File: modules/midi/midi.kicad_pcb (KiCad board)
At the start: 2 copper layers, 30.5 x 68.6 mm, 57 parts, among them J1 MIDI_IN, U1 ATtiny1616-M

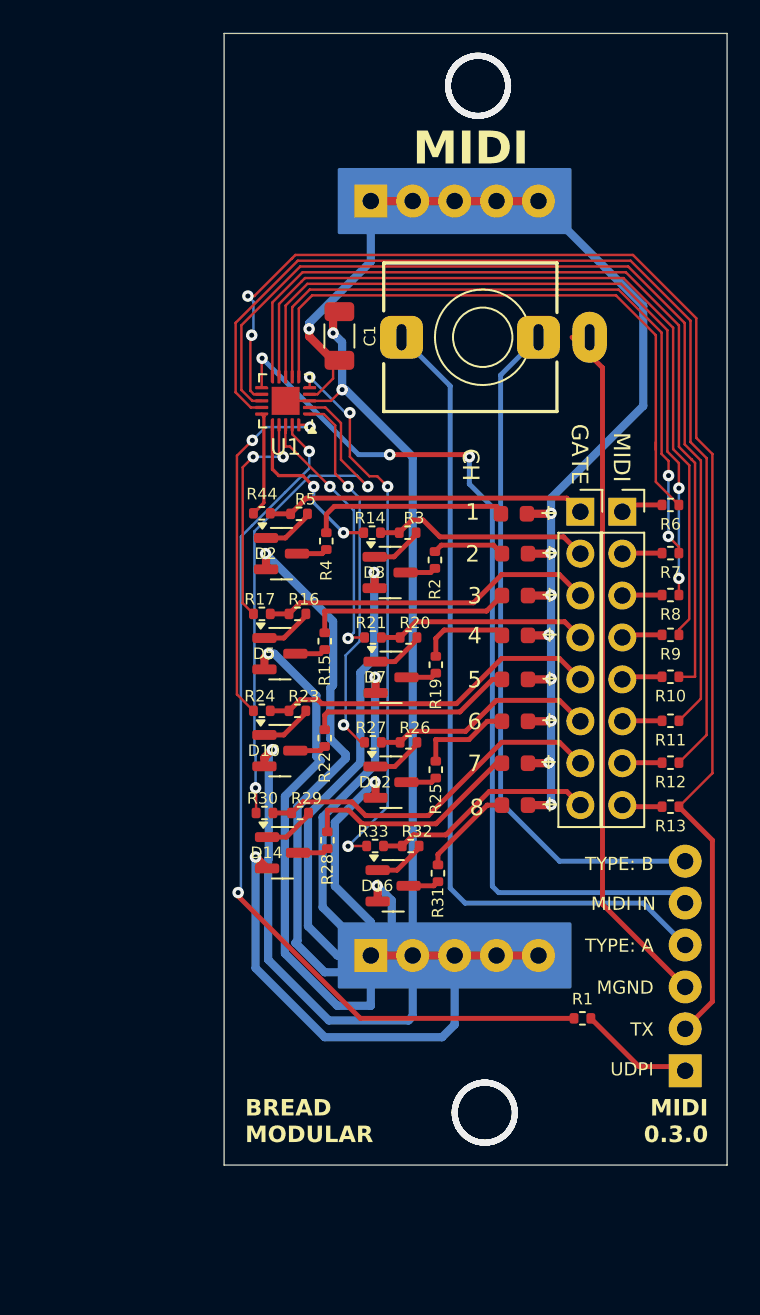
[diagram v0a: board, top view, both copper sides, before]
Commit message: midi: Connect MIDI ground to common GND
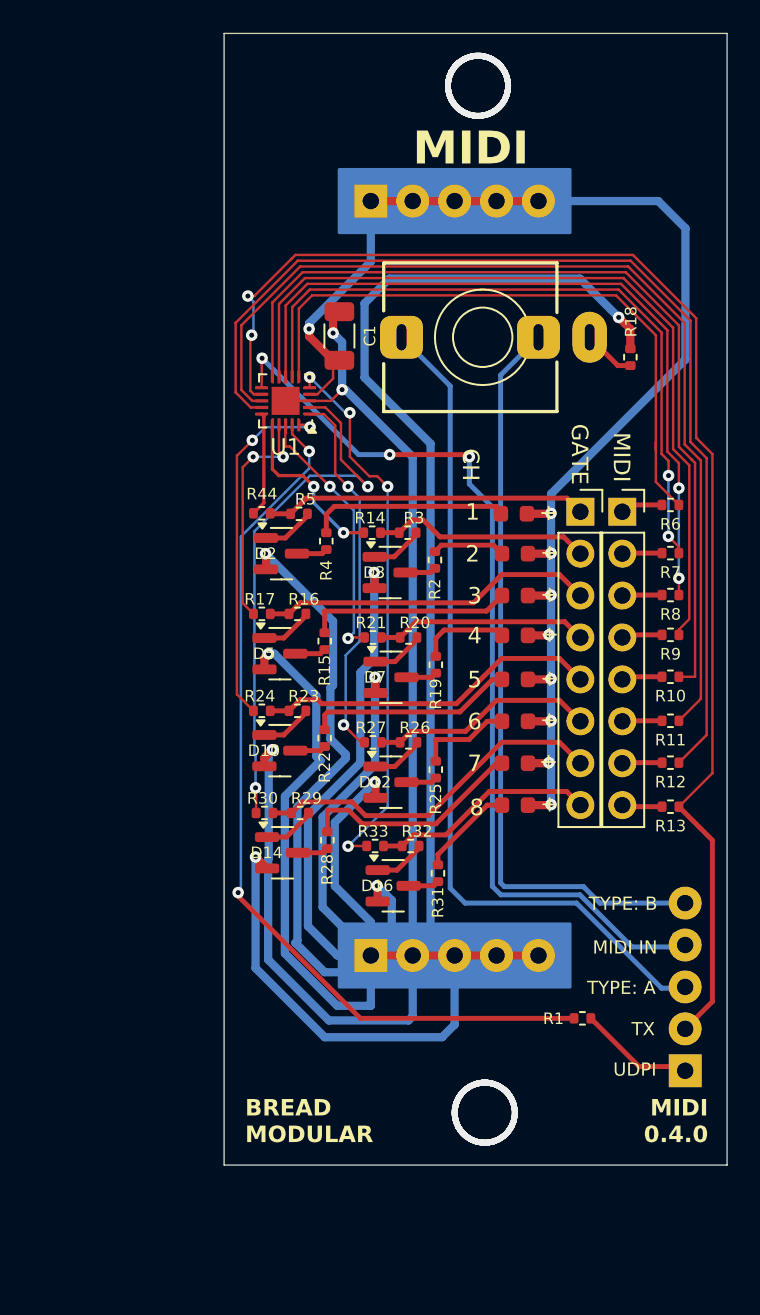
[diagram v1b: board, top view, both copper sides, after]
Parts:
- added R18: 10k, Resistor_SMD:R_0402_1005Metric, F.Cu at (71.6, 60.3)
- CONFIG1: footprint BreadModular_MISC:Conn_Holes_6 -> BreadModular_MISC:Power_Connector
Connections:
- CONFIG1 pad 3: MIDI_GROUND -> MIDI_DATA_TYPE_A
- CONFIG1 pad 4: MIDI_DATA_TYPE_A -> MIDI_IN
- CONFIG1 pad 5: MIDI_IN -> MIDI_DATA_TYPE_B
- J1 pad S: MIDI_GROUND -> Net-(J1-PadS)
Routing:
- net GND: track 242.4 -> 303.1 mm, vias 10 -> 11
- net MIDI_GROUND: track 42.3 -> 0.00 mm
- net V_SUPPLY: track 77.5 -> 83.9 mm
- net MIDI_DATA_TYPE_B: track 41.8 -> 45.7 mm
- net Net-(J1-PadS): track 0.00 -> 3.18 mm
- net MIDI_IN: track 55.3 -> 57.3 mm
- net MIDI_DATA_TYPE_A: track 50.0 -> 51.4 mm
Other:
- board text added: "MIDI 0.4.0"
- board text removed: "MGND"
- board text removed: "MIDI 0.3.0"

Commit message: midi: fix instability in MIDI recieving
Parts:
- removed R18: 10k, Resistor_SMD:R_0402_1005Metric
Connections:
- J1 pad S: Net-(J1-PadS) -> GND
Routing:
- net Net-(J1-PadS): track 3.18 -> 0.00 mm
- net GND: track 303.1 -> 301.7 mm, vias 11 -> 10
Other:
- board text added: "MIDI 0.5.0"
- board text removed: "MIDI 0.4.0"
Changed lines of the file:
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@@
 	(net 62 "Net-(D100-K)")
 	(net 63 "MIDI_DATA_TYPE_A")
-	(net 64 "Net-(J1-PadS)")
 	(footprint "LED_SMD:LED_0603_1608Metric"
 		(layer "F.Cu")
@@
 			(layers "*.Cu" "*.Mask")
 			(remove_unused_layers no)
-			(net 64 "Net-(J1-PadS)")
+			(net 1 "GND")
 			(pintype "passive")
 		)
@@
 		)
 	)
-	(footprint "Resistor_SMD:R_0402_1005Metric"
-		(layer "F.Cu")
-		(at 71.61 60.26 90)
-		(descr "Resistor SMD 0402 (1005 Metric), square (rectangular) end terminal, IPC_7351 nominal, (Body size source: IPC-SM-782 page 72, https://www.pcb-3d.com/wordpress/wp-content/uploads/ipc-sm-782a_amendment_1_and_2.pdf), generated with kicad-footprint-generator")
-		(tags "resistor")
-		(property "Reference" "R18"
-			(at 2.15 0.04 90)
-			(layer "F.SilkS")
-			(effects
-				(font
-					(size 0.7 0.7)
-					(thickness 0.1)
-				)
-			)
-		)
-		(property "Value" "10k"
-			(at 0 1.17 90)
-			(layer "F.Fab")
-			(effects
-				(font
-					(size 1 1)
-					(thickness 0.15)
-				)
-			)
-		)
-		(property "Footprint" "Resistor_SMD:R_0402_1005Metric"
-			(at 0 0 90)
-			(unlocked yes)
-			(layer "F.Fab")
-			(hide yes)
-			(effects
-				(font
-					(size 1.27 1.27)
-					(thickness 0.15)
-				)
-			)
-		)
-		(property "Datasheet" ""
-			(at 0 0 90)
-			(unlocked yes)
-			(layer "F.Fab")
-			(hide yes)
-			(effects
-				(font
-					(size 1.27 1.27)
-					(thickness 0.15)
-				)
-			)
-		)
-		(property "Description" "Resistor"
-			(at 0 0 90)
-			(unlocked yes)
-			(layer "F.Fab")
-			(hide yes)
-			(effects
-				(font
-					(size 1.27 1.27)
-					(thickness 0.15)
-				)
-			)
-		)
-		(property ki_fp_filters "R_*")
-		(sheetname "Root")
-		(sheetfile "midi.kicad_sch")
-		(attr smd)
-		(fp_line
-			(start -0.153641 -0.38)
-			(end 0.153641 -0.38)
-			(stroke
-				(width 0.12)
-				(type solid)
-			)
-			(layer "F.SilkS")
-		)
-		(fp_line
-			(start -0.153641 0.38)
-			(end 0.153641 0.38)
-			(stroke
-				(width 0.12)
-				(type solid)
-			)
-			(layer "F.SilkS")
-		)
-		(fp_line
-			(start 0.93 -0.47)
-			(end 0.93 0.47)
-			(stroke
-				(width 0.05)
-				(type solid)
-			)
-			(layer "F.CrtYd")
-		)
-		(fp_line
-			(start -0.93 -0.47)
-			(end 0.93 -0.47)
-			(stroke
-				(width 0.05)
-				(type solid)
-			)
-			(layer "F.CrtYd")
-		)
-		(fp_line
-			(start 0.93 0.47)
-			(end -0.93 0.47)
-			(stroke
-				(width 0.05)
-				(type solid)
-			)
-			(layer "F.CrtYd")
-		)
-		(fp_line
-			(start -0.93 0.47)
-			(end -0.93 -0.47)
-			(stroke
-				(width 0.05)
-				(type solid)
-			)
-			(layer "F.CrtYd")
-		)
-		(fp_line
-			(start 0.525 -0.27)
-			(end 0.525 0.27)
-			(stroke
-				(width 0.1)
-				(type solid)
-			)
-			(layer "F.Fab")
-		)
-		(fp_line
-			(start -0.525 -0.27)
-			(end 0.525 -0.27)
-			(stroke
-				(width 0.1)
-				(type solid)
-			)
-			(layer "F.Fab")
-		)
-		(fp_line
-			(start 0.525 0.27)
-			(end -0.525 0.27)
-			(stroke
-				(width 0.1)
-				(type solid)
-			)
-			(layer "F.Fab")
-		)
-		(fp_line
-			(start -0.525 0.27)
-			(end -0.525 -0.27)
-			(stroke
-				(width 0.1)
-				(type solid)
-			)
-			(layer "F.Fab")
-		)
-		(fp_text user "${REFERENCE}"
-			(at 0 0 90)
-			(layer "F.Fab")
-			(effects
-				(font
-					(size 0.26 0.26)
-					(thickness 0.04)
-				)
-			)
-		)
-		(pad "1" smd roundrect
-			(at -0.51 0 90)
-			(size 0.54 0.64)
-			(layers "F.Cu" "F.Paste" "F.Mask")
-			(roundrect_rratio 0.25)
-			(net 64 "Net-(J1-PadS)")
-			(pintype "passive")
-		)
-		(pad "2" smd roundrect
-			(at 0.51 0 90)
-			(size 0.54 0.64)
-			(layers "F.Cu" "F.Paste" "F.Mask")
-			(roundrect_rratio 0.25)
-			(net 1 "GND")
-			(pintype "passive")
-		)
-		(model "${KICAD8_3DMODEL_DIR}/Resistor_SMD.3dshapes/R_0402_1005Metric.wrl"
-			(offset
-				(xyz 0 0 0)
-			)
-			(scale
-				(xyz 1 1 1)
-			)
-			(rotate
-				(xyz 0 0 0)
-			)
-		)
-	)
 	(footprint "Package_TO_SOT_SMD:SOT-23"
 		(layer "F.Cu")
@@
 		)
 	)
-	(gr_text "MIDI\n0.4.0"
+	(gr_text "MIDI\n0.5.0"
 		(at 76.327 107.95 0)
 		(layer "F.SilkS")
@@
 	)
 	(segment
-		(start 71.61 58.56)
-		(end 70.9 57.85)
-		(width 0.5)
-		(layer "F.Cu")
-		(net 1)
-	)
-	(segment
 		(start 50.717 62.909)
 		(end 52.167 62.909)
@@
 	)
 	(segment
-		(start 71.61 59.5)
-		(end 71.61 58.56)
-		(width 0.5)
-		(layer "F.Cu")
-		(net 1)
-	)
-	(segment
 		(start 49.911 84.0486)
 		(end 49.431 84.5286)
@@
 		(net 1)
 	)
-	(via
-		(at 70.9 57.85)
-		(size 0.7)
-		(drill 0.3)
-		(layers "F.Cu" "B.Cu")
-		(net 1)
-	)
 	(segment
 		(start 52.578 84.455)
@@
 	)
 	(segment
-		(start 70.9 57.85)
-		(end 68.55 55.5)
-		(width 0.5)
-		(layer "B.Cu")
-		(net 1)
-	)
-	(segment
 		(start 54.14 62.23)
 		(end 54.14 59.347)
@@
 	)
 	(segment
+		(start 69.14 56.09)
+		(end 69.14 59.055)
+		(width 0.5)
+		(layer "B.Cu")
+		(net 1)
+	)
+	(segment
 		(start 49.695 90.64)
 		(end 49.657 90.678)
@@
 	)
 	(segment
+		(start 68.55 55.5)
+		(end 69.14 56.09)
+		(width 0.5)
+		(layer "B.Cu")
+		(net 1)
+	)
+	(segment
 		(start 55.5 61.5)
 		(end 59.5 65.5)
@@
 		(net 63)
 	)
-	(segment
-		(start 71.61 60.77)
-		(end 70.855 60.77)
-		(width 0.3)
-		(layer "F.Cu")
-		(net 64)
-	)
-	(segment
-		(start 70.855 60.77)
-		(end 69.14 59.055)
-		(width 0.3)
-		(layer "F.Cu")
-		(net 64)
-	)
 )

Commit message: midi_1.0.0
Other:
- board text added: "MIDI 1.0.0"
- board text removed: "MIDI 0.5.0"
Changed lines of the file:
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@@
 		)
 	)
-	(gr_text "MIDI\n0.5.0"
+	(gr_text "MIDI\n1.0.0"
 		(at 76.327 107.95 0)
 		(layer "F.SilkS")

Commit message: midi: Change udpi to updi in action
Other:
- board text added: "MIDI 1.0.1"
- board text added: "UPDI"
- board text removed: "MIDI 1.0.0"
- board text removed: "UDPI"
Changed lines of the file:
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@@
 		)
 	)
-	(gr_text "MIDI\n1.0.0"
+	(gr_text "MIDI\n1.0.1"
 		(at 76.327 107.95 0)
 		(layer "F.SilkS")
@@
 		)
 	)
-	(gr_text "UDPI"
+	(gr_text "UPDI"
 		(at 73.2 103.9 0)
 		(layer "F.SilkS")

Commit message: Add opto-couplers for the midi input
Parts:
- added C2: 0.1uf, Capacitor_SMD:C_0402_1005Metric, F.Cu at (62.3, 99.9)
- added D9: SS14, Diode_SMD:D_SMA, F.Cu at (68.0, 105.0)
- added R18: 220, Resistor_SMD:R_0402_1005Metric, F.Cu at (70.9, 107.0)
- added R34: 10k, Resistor_SMD:R_0402_1005Metric, F.Cu at (62.3, 101.3)
- added U2: 6N137, BreadModular_MISC:SOIC-8 2.54, F.Cu at (53.0, 103.6)
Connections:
- J1 pad S: GND -> MIDI_GROUND
- U1 pad 11: MIDI_IN -> MIDI_INVERTED
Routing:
- net MIDI_GROUND: track 0.00 -> 72.6 mm, vias 0 -> 3
- net MIDI_INVERTED: track 0.00 -> 72.6 mm, vias 0 -> 6
- net GND: track 301.7 -> 251.9 mm, vias 10 -> 12
- net MIDI_IN: track 57.3 -> 14.3 mm, vias 3 -> 2
- net V_SUPPLY: track 83.9 -> 116.6 mm, vias 9 -> 11
- net Net-(D9-K): track 0.00 -> 30.9 mm
- net Net-(U1-~{RESET}/PA0): track 54.2 -> 57.2 mm
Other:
- board text added: "MIDI 2.0.0"
- board text removed: "MIDI 1.0.1"
